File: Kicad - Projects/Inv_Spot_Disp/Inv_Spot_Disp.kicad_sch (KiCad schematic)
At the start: 44 parts, among them J1 PWM_Out, J2 Power_Supply, J3 Current_Sense, J4 Prog, SW1 1, SW2 2, SW3 3, SW4 4, SW5 SW_Push, U1 STM32F030F4Px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

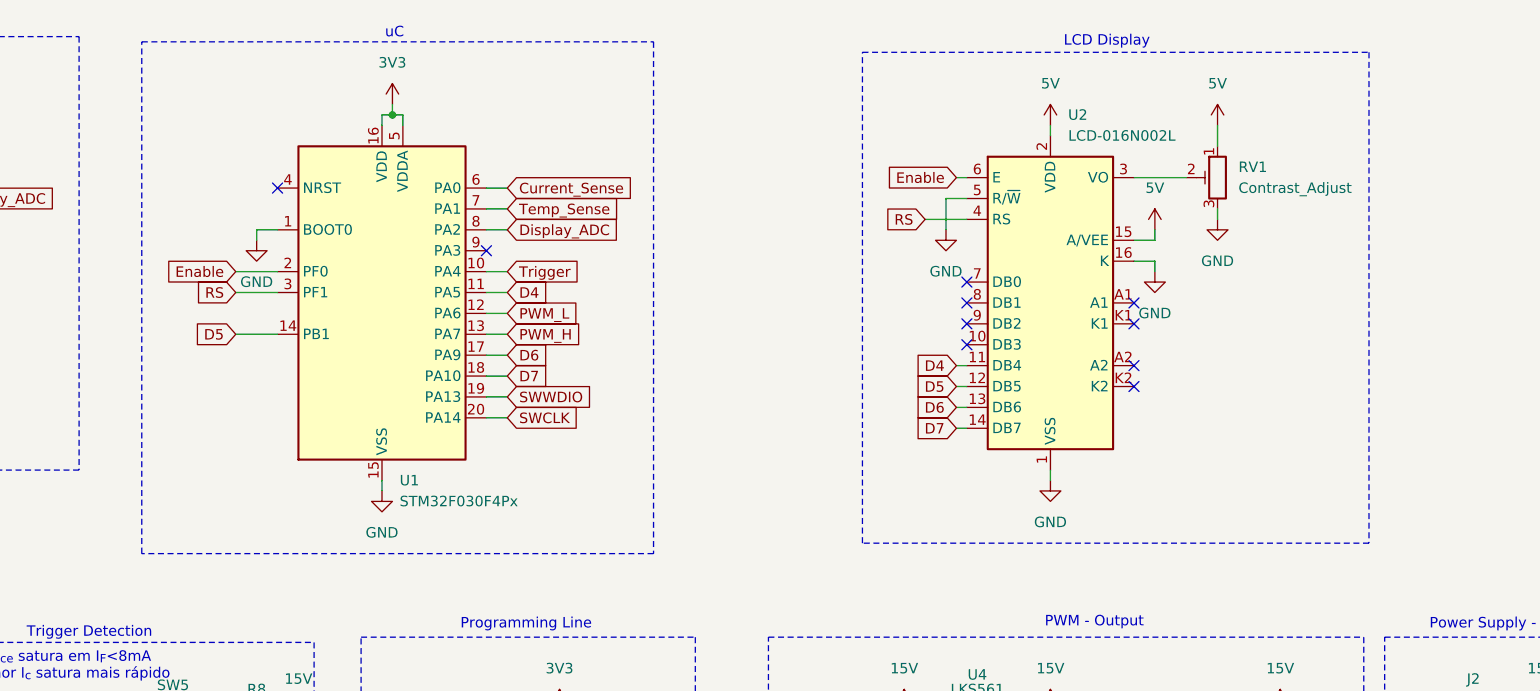
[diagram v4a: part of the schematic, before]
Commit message: Corrigido Footprint do Display
Corrigido problema com o footprint do display

Melhora o caminho de retorna das trilhas de programação

Aumento na quantidade de vias para reduzir impedância do plano terra
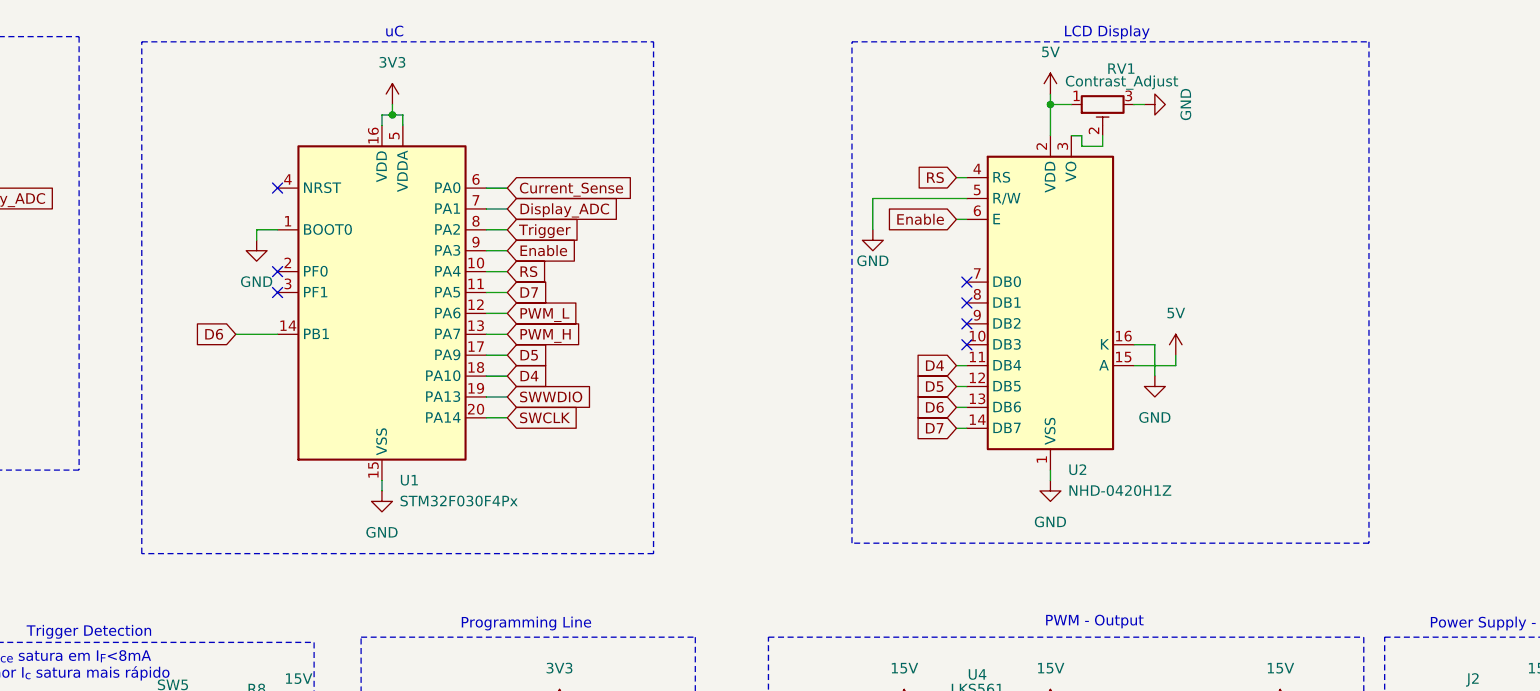
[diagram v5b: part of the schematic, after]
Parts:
- removed U2: LCD-016N002L, Display:LCD-016N002L, symbol Display_Character:LCD-016N002L
- added U2: NHD-0420H1Z, Display:WC1602A, symbol Display_Character:NHD-0420H1Z
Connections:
- net Temp_Sense is gone; now on net Display_ADC: U1.7 (PA1)
- net 5V: now also U2.15 (A), U2.2 (VDD)
- net D4: now also U1.18 (PA10), U2.11 (DB4); no longer U1.11 (PA5)
- net D5: now also U1.17 (PA9), U2.12 (DB5); no longer U1.14 (PB1)
- net D6: now also U1.14 (PB1), U2.13 (DB6); no longer U1.17 (PA9)
- net D7: now also U1.11 (PA5), U2.14 (DB7); no longer U1.18 (PA10)
- net Display_ADC: no longer U1.8 (PA2)
- net Enable: now also U1.9 (PA3), U2.6 (E); no longer U1.2 (PF0)
- net GND: now also U2.1 (VSS), U2.16 (K), U2.5 (R/W)
- net RS: now also U1.10 (PA4), U2.4 (RS); no longer U1.3 (PF1)
- net Trigger: now also U1.8 (PA2); no longer U1.10 (PA4)
- net at RV1.2: now also U2.3 (VO)
- no-connect marks 10 -> 7
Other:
- moved on the sheet: RV1
